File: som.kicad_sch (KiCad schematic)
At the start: 35 parts, among them M1 jetson-orin-nx/nano-module, U4 NTS0102GT

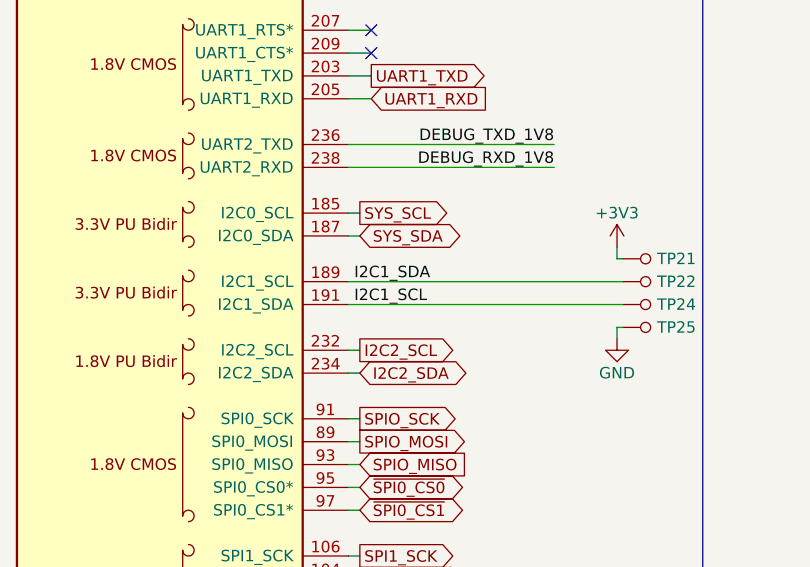
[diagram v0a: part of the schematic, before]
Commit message: Fixed I2C label swap [#40595]
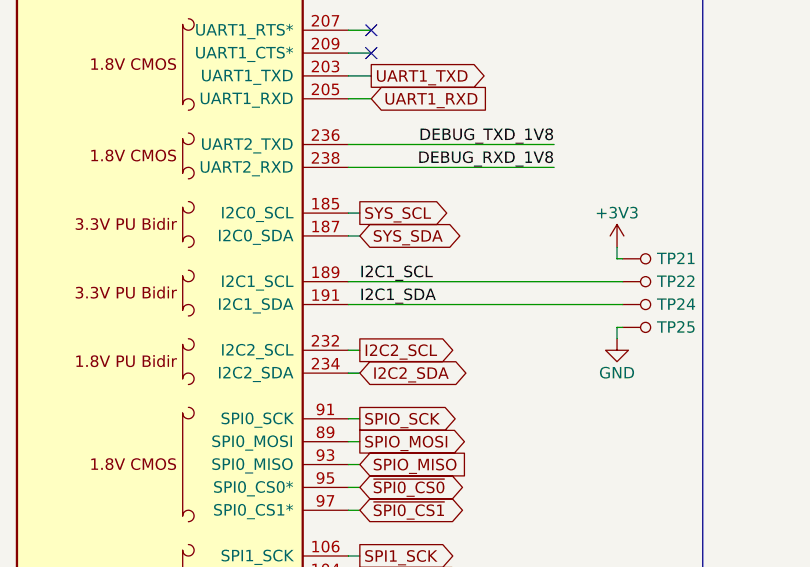
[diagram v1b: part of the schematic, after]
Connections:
- net I2C1_SCL: now also A1.189 (I2C1_SCL), TP22.1; no longer A1.191 (I2C1_SDA), TP24.1
- net I2C1_SDA: now also A1.191 (I2C1_SDA), TP24.1; no longer A1.189 (I2C1_SCL), TP22.1
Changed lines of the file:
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@@
     (effects (font (size 1.27 1.27)) (justify left bottom))
   )
-  (label "I2C1_SCL" (at 189.865 73.66 0)
+  (label "I2C1_SCL" (at 190.5 71.12 0)
     (effects (font (size 1.27 1.27)) (justify left bottom))
   )
-  (label "I2C1_SDA" (at 189.865 71.12 0)
+  (label "I2C1_SDA" (at 190.5 73.66 0)
     (effects (font (size 1.27 1.27)) (justify left bottom))
   )

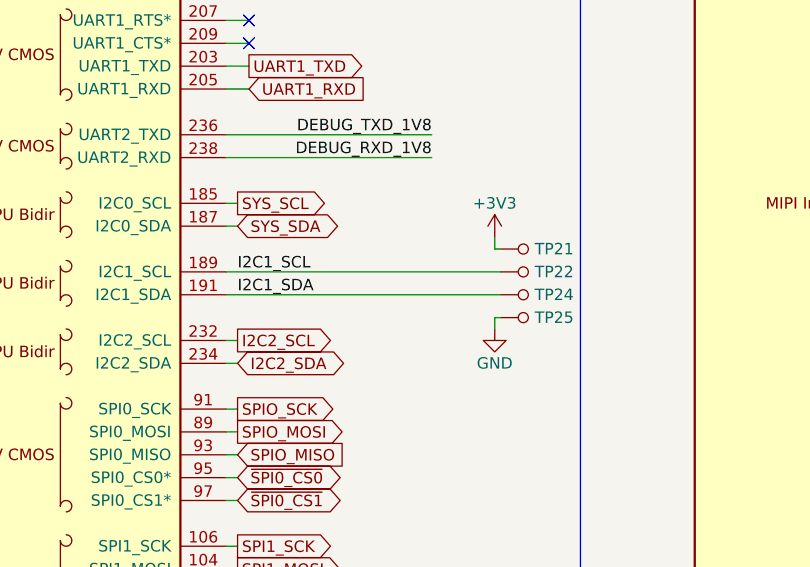
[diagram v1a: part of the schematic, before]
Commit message: Added I2C connector [#40797]
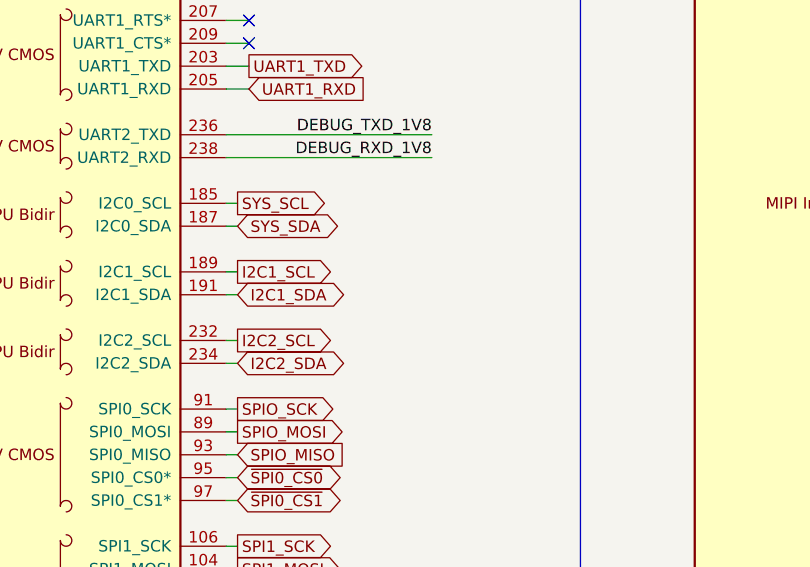
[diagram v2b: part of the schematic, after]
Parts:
- removed TP21, TP22, TP24, TP25: TP_SMD_0_75MM, jetson-orin-baseboard-footprints:Testpoint_smd_0_75mm, symbol jetson-orin-baseboard:TP_SMD_0_75MM
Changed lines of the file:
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@@
     (stroke (width 0) (type default) (color 0 0 0 0))
   )
+  (wire (pts (xy 190.5 73.66) (xy 189.23 73.66))
+    (stroke (width 0) (type default) (color 0 0 0 0))
+  )
   (wire (pts (xy 114.3 35.56) (xy 87.63 35.56))
     (stroke (width 0) (type default) (color 0 0 0 0))
@@
     (stroke (width 0) (type default) (color 0 0 0 0))
   )
-  (wire (pts (xy 219.075 76.2) (xy 219.075 77.47))
-    (stroke (width 0) (type default) (color 0 0 0 0))
-  )
   (wire (pts (xy 189.23 195.58) (xy 194.31 195.58))
     (stroke (width 0) (type default) (color 0 0 0 0))
@@
     (stroke (width 0) (type default) (color 0 0 0 0))
   )
-  (wire (pts (xy 189.23 71.12) (xy 219.71 71.12))
-    (stroke (width 0) (type default) (color 0 0 0 0))
-  )
   (wire (pts (xy 49.53 104.14) (xy 50.8 104.14))
     (stroke (width 0) (type default) (color 0 0 0 0))
@@
     (stroke (width 0) (type default) (color 0 0 0 0))
   )
+  (wire (pts (xy 190.5 71.12) (xy 189.23 71.12))
+    (stroke (width 0) (type default) (color 0 0 0 0))
+  )
   (wire (pts (xy 105.41 64.77) (xy 114.3 64.77))
     (stroke (width 0) (type default) (color 0 0 0 0))
@@
     (stroke (width 0) (type default) (color 0 0 0 0))
   )
-  (wire (pts (xy 219.075 67.31) (xy 219.075 68.58))
-    (stroke (width 0) (type default) (color 0 0 0 0))
-  )
   (wire (pts (xy 49.53 88.9) (xy 50.8 88.9))
     (stroke (width 0) (type default) (color 0 0 0 0))
@@
     (stroke (width 0) (type default) (color 0 0 0 0))
   )
-  (wire (pts (xy 189.23 73.66) (xy 219.71 73.66))
-    (stroke (width 0) (type default) (color 0 0 0 0))
-  )
   (wire (pts (xy 367.03 114.3) (xy 377.19 114.3))
     (stroke (width 0) (type default) (color 0 0 0 0))
@@
     (stroke (width 0) (type default) (color 0 0 0 0))
   )
-  (wire (pts (xy 219.71 76.2) (xy 219.075 76.2))
-    (stroke (width 0) (type default) (color 0 0 0 0))
-  )
   (wire (pts (xy 190.5 104.14) (xy 189.23 104.14))
     (stroke (width 0) (type default) (color 0 0 0 0))
@@
     (stroke (width 0) (type default) (color 0 0 0 0))
   )
-  (wire (pts (xy 219.71 68.58) (xy 219.075 68.58))
-    (stroke (width 0) (type default) (color 0 0 0 0))
-  )
   (wire (pts (xy 377.19 93.98) (xy 367.03 93.98))
     (stroke (width 0) (type default) (color 0 0 0 0))
@@
     (effects (font (size 1.27 1.27)) (justify left bottom))
   )
-  (label "I2C1_SCL" (at 190.5 71.12 0)
-    (effects (font (size 1.27 1.27)) (justify left bottom))
-  )
-  (label "I2C1_SDA" (at 190.5 73.66 0)
-    (effects (font (size 1.27 1.27)) (justify left bottom))
-  )
   (label "SoM_5V_IN" (at 49.53 86.36 180)
     (effects (font (size 1.27 1.27)) (justify right bottom))
@@
     )
   )
+  (global_label "I2C1_SCL" (shape output) (at 190.5 71.12 0)
+    (effects (font (size 1.27 1.27)) (justify left))
+    (property "Intersheet References" "${INTERSHEET_REFS}" (id 0) (at 204.47 71.12 0)
+      (effects (font (size 1.27 1.27)) (justify left))
+    )
+  )
   (global_label "USBSS1_RX_N" (shape output) (at 194.31 205.74 0)
     (effects (font (size 1.27 1.27)) (justify left))
@@
     )
   )
+  (global_label "I2C1_SDA" (shape bidirectional) (at 190.5 73.66 0)
+    (effects (font (size 1.27 1.27)) (justify left))
+    (property "Intersheet References" "${INTERSHEET_REFS}" (id 0) (at 204.47 73.66 0)
+      (effects (font (size 1.27 1.27)) (justify left))
+    )
+  )
   (global_label "USB0_D_N" (shape output) (at 194.31 226.06 0)
     (effects (font (size 1.27 1.27)) (justify left))
@@
     (pin "1")
   )
-  (symbol (lib_id "jetson-orin-baseboard:TP_SMD_0_75MM") (at 222.25 73.66 90) (unit 1)
-    (in_bom yes) (on_board yes) (fields_autoplaced)
-    (property "Reference" "TP24" (id 0) (at 223.52 73.6599 90)
-      (effects (font (size 1.27 1.27)) (justify right))
-    )
-    (property "Value" "TP_SMD_0_75MM" (id 1) (at 224.79 73.66 0)
-      (effects (font (size 1.27 1.27)) hide)
-    )
-    (property "Footprint" "jetson-orin-baseboard-footprints:Testpoint_smd_0_75mm" (id 2) (at 217.17 68.58 0)
-      (effects (font (size 1.524 1.524)) (justify left) hide)
-    )
-    (property "Datasheet" "" (id 3) (at 214.63 68.58 0)
-      (effects (font (size 1.524 1.524)) (justify left) hide)
-    )
-    (pin "1")
-  )
   (symbol (lib_id "jetson-orin-baseboard:GND") (at 30.48 101.6 0) (unit 1)
     (in_bom yes) (on_board yes) (fields_autoplaced)
@@
     (pin "1")
   )
-  (symbol (lib_id "jetson-orin-baseboard:TP_SMD_0_75MM") (at 222.25 76.2 90) (unit 1)
-    (in_bom yes) (on_board yes) (fields_autoplaced)
-    (property "Reference" "TP25" (id 0) (at 223.52 76.1999 90)
-      (effects (font (size 1.27 1.27)) (justify right))
-    )
-    (property "Value" "TP_SMD_0_75MM" (id 1) (at 224.79 76.2 0)
-      (effects (font (size 1.27 1.27)) hide)
-    )
-    (property "Footprint" "jetson-orin-baseboard-footprints:Testpoint_smd_0_75mm" (id 2) (at 217.17 71.12 0)
-      (effects (font (size 1.524 1.524)) (justify left) hide)
-    )
-    (property "Datasheet" "" (id 3) (at 214.63 71.12 0)
-      (effects (font (size 1.524 1.524)) (justify left) hide)
-    )
-    (pin "1")
-  )
   (symbol (lib_id "jetson-orin-baseboard:R_0R_0402") (at 101.6 64.77 0) (unit 1)
     (in_bom yes) (on_board yes)
@@
     (pin "2")
   )
-  (symbol (lib_id "jetson-orin-baseboard:+3V3") (at 219.075 67.31 0) (unit 1)
-    (in_bom yes) (on_board yes)
-    (property "Reference" "#PWR0184" (id 0) (at 219.075 71.12 0)
-      (effects (font (size 1.27 1.27)) hide)
-    )
-    (property "Value" "+3V3" (id 1) (at 219.075 63.5 0))
-    (property "Footprint" "" (id 2) (at 219.075 67.31 0)
-      (effects (font (size 1.27 1.27)) hide)
-    )
-    (property "Datasheet" "" (id 3) (at 219.075 67.31 0)
-      (effects (font (size 1.27 1.27)) hide)
-    )
-    (pin "1")
-  )
   (symbol (lib_id "jetson-orin-baseboard:Jetson-Orin-9.2H-socket") (at 273.05 25.4 0) (mirror y) (unit 2)
     (in_bom yes) (on_board yes)
@@
     (pin "2")
   )
-  (symbol (lib_id "jetson-orin-baseboard:TP_SMD_0_75MM") (at 222.25 71.12 90) (unit 1)
-    (in_bom yes) (on_board yes) (fields_autoplaced)
-    (property "Reference" "TP22" (id 0) (at 223.52 71.1199 90)
-      (effects (font (size 1.27 1.27)) (justify right))
-    )
-    (property "Value" "TP_SMD_0_75MM" (id 1) (at 224.79 71.12 0)
-      (effects (font (size 1.27 1.27)) hide)
-    )
-    (property "Footprint" "jetson-orin-baseboard-footprints:Testpoint_smd_0_75mm" (id 2) (at 217.17 66.04 0)
-      (effects (font (size 1.524 1.524)) (justify left) hide)
-    )
-    (property "Datasheet" "" (id 3) (at 214.63 66.04 0)
-      (effects (font (size 1.524 1.524)) (justify left) hide)
-    )
-    (pin "1")
-  )
   (symbol (lib_id "jetson-orin-baseboard:MS621FE-FL11E") (at 45.72 142.24 0) (mirror y) (unit 1)
     (in_bom yes) (on_board yes) (fields_autoplaced)
@@
     (pin "-")
   )
-  (symbol (lib_id "jetson-orin-baseboard:GND") (at 219.075 77.47 0) (unit 1)
-    (in_bom yes) (on_board yes) (fields_autoplaced)
-    (property "Reference" "#PWR0185" (id 0) (at 219.075 83.82 0)
-      (effects (font (size 1.27 1.27)) hide)
-    )
-    (property "Value" "GND" (id 1) (at 219.075 81.28 0))
-    (property "Footprint" "" (id 2) (at 219.075 77.47 0)
-      (effects (font (size 1.27 1.27)) hide)
-    )
-    (property "Datasheet" "" (id 3) (at 219.075 77.47 0)
-      (effects (font (size 1.27 1.27)) hide)
-    )
-    (pin "1")
-  )
-  (symbol (lib_id "jetson-orin-baseboard:TP_SMD_0_75MM") (at 222.25 68.58 90) (unit 1)
-    (in_bom yes) (on_board yes) (fields_autoplaced)
-    (property "Reference" "TP21" (id 0) (at 223.52 68.5799 90)
-      (effects (font (size 1.27 1.27)) (justify right))
-    )
-    (property "Value" "TP_SMD_0_75MM" (id 1) (at 224.79 68.58 0)
-      (effects (font (size 1.27 1.27)) hide)
-    )
-    (property "Footprint" "jetson-orin-baseboard-footprints:Testpoint_smd_0_75mm" (id 2) (at 217.17 63.5 0)
-      (effects (font (size 1.524 1.524)) (justify left) hide)
-    )
-    (property "Datasheet" "" (id 3) (at 214.63 63.5 0)
-      (effects (font (size 1.524 1.524)) (justify left) hide)
-    )
-    (pin "1")
-  )
   (symbol (lib_id "jetson-orin-baseboard:GND") (at 35.56 101.6 0) (unit 1)

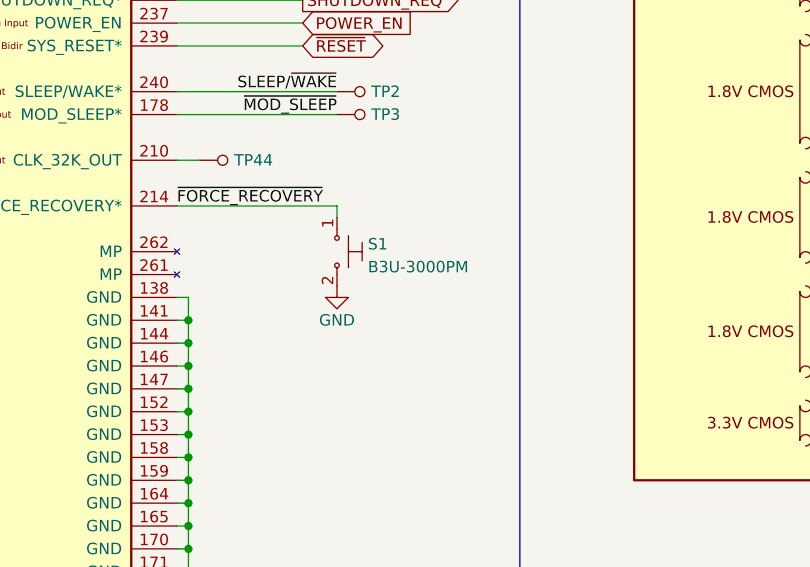
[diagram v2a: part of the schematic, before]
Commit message: Replace buttons with top-actuated ones
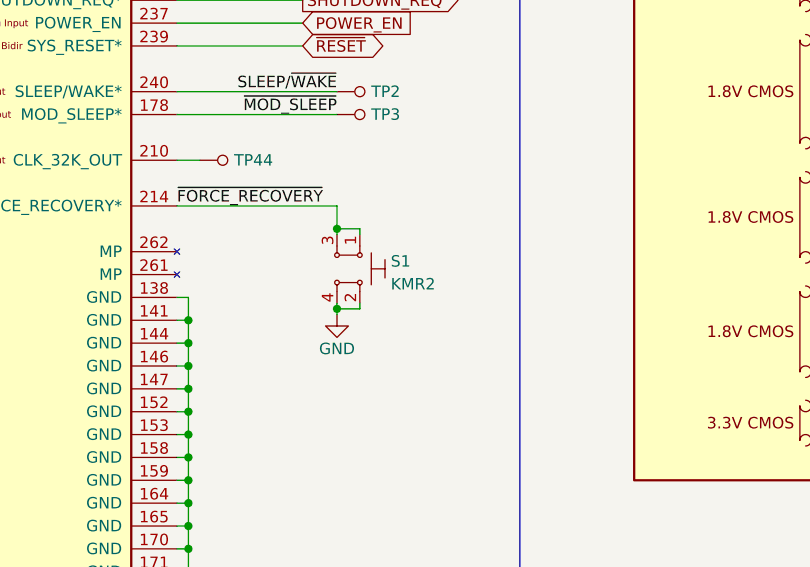
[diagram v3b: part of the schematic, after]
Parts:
- removed S1: B3U-3000PM, jetson-orin-baseboard-footprints:B3U-3000P, symbol jetson-orin-baseboard:B3U-3000PM
- added S1: KMR2, antmicro-footprints:SW_SPST_4.2x2.8, symbol antmicroPushbuttonSwitches:KMR2
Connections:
- net GND: now also S1.2, S1.4
- net ~{FORCE_RECOVERY}: now also S1.1, S1.3
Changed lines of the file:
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@@
   (junction (at 49.53 93.98) (diameter 0) (color 0 0 0 0)
   )
+  (junction (at 119.38 121.92) (diameter 0) (color 0 0 0 0)
+  )
   (junction (at 49.53 180.34) (diameter 0) (color 0 0 0 0)
   )
@@
   (junction (at 49.53 134.62) (diameter 0) (color 0 0 0 0)
   )
+  (junction (at 119.38 130.81) (diameter 0) (color 0 0 0 0)
+  )
   (junction (at 49.53 190.5) (diameter 0) (color 0 0 0 0)
   )
@@
     (stroke (width 0) (type default) (color 0 0 0 0))
   )
+  (wire (pts (xy 119.38 130.175) (xy 119.38 130.81))
+    (stroke (width 0) (type default) (color 0 0 0 0))
+  )
   (wire (pts (xy 377.19 223.52) (xy 367.03 223.52))
     (stroke (width 0) (type default) (color 0 0 0 0))
@@
     (stroke (width 0) (type default) (color 0 0 0 0))
   )
+  (wire (pts (xy 119.38 130.81) (xy 119.38 131.445))
+    (stroke (width 0) (type default) (color 0 0 0 0))
+  )
   (wire (pts (xy 190.5 71.12) (xy 189.23 71.12))
     (stroke (width 0) (type default) (color 0 0 0 0))
@@
     (stroke (width 0) (type default) (color 0 0 0 0))
   )
+  (wire (pts (xy 119.38 121.92) (xy 119.38 122.555))
+    (stroke (width 0) (type default) (color 0 0 0 0))
+  )
   (wire (pts (xy 101.6 129.54) (xy 102.87 129.54))
     (stroke (width 0) (type default) (color 0 0 0 0))
@@
     (stroke (width 0) (type default) (color 0 0 0 0))
   )
+  (wire (pts (xy 119.38 121.92) (xy 121.92 121.92))
+    (stroke (width 0) (type default) (color 0 0 0 0))
+  )
   (wire (pts (xy 114.3 38.1) (xy 87.63 38.1))
     (stroke (width 0) (type default) (color 0 0 0 0))
@@
     (stroke (width 0) (type default) (color 0 0 0 0))
   )
+  (wire (pts (xy 121.92 121.92) (xy 121.92 122.555))
+    (stroke (width 0) (type default) (color 0 0 0 0))
+  )
   (wire (pts (xy 93.98 250.19) (xy 93.98 251.46))
     (stroke (width 0) (type default) (color 0 0 0 0))
@@
     (stroke (width 0) (type default) (color 0 0 0 0))
   )
+  (wire (pts (xy 119.38 130.81) (xy 121.92 130.81))
+    (stroke (width 0) (type default) (color 0 0 0 0))
+  )
   (wire (pts (xy 377.19 149.86) (xy 367.03 149.86))
     (stroke (width 0) (type default) (color 0 0 0 0))
@@
     (stroke (width 0) (type default) (color 0 0 0 0))
   )
+  (wire (pts (xy 121.92 130.81) (xy 121.92 130.175))
+    (stroke (width 0) (type default) (color 0 0 0 0))
+  )
   (wire (pts (xy 49.53 182.88) (xy 49.53 180.34))
     (stroke (width 0) (type default) (color 0 0 0 0))
@@
     (stroke (width 0) (type default) (color 0 0 0 0))
   )
+  (wire (pts (xy 119.38 119.38) (xy 119.38 121.92))
+    (stroke (width 0) (type default) (color 0 0 0 0))
+  )
   (wire (pts (xy 101.6 193.04) (xy 102.87 193.04))
     (stroke (width 0) (type default) (color 0 0 0 0))
@@
     (stroke (width 0) (type default) (color 0 0 0 0))
   )
-  (wire (pts (xy 119.38 119.38) (xy 119.38 120.65))
-    (stroke (width 0) (type default) (color 0 0 0 0))
-  )
   (wire (pts (xy 189.23 243.84) (xy 194.31 243.84))
     (stroke (width 0) (type default) (color 0 0 0 0))
@@
     (pin "1")
   )
+  (symbol (lib_id "antmicroPushbuttonSwitches:KMR2") (at 121.92 126.365 270) (unit 1)
+    (in_bom yes) (on_board yes) (fields_autoplaced)
+    (property "Reference" "S1" (id 0) (at 125.349 125.5303 90)
+      (effects (font (size 1.27 1.27)) (justify left))
+    )
+    (property "Value" "KMR2" (id 1) (at 125.349 128.0672 90)
+      (effects (font (size 1.27 1.27)) (justify left))
+    )
+    (property "Footprint" "antmicro-footprints:SW_SPST_4.2x2.8" (id 2) (at 127 131.445 0)
+      (effects (font (size 1.27 1.27)) (justify left) hide)
+    )
+    (property "Datasheet" "http://www.farnell.com/datasheets/2631211.pdf" (id 3) (at 129.54 131.445 0)
+      (effects (font (size 1.524 1.524)) (justify left) hide)
+    )
+    (property "MPN" "KMR211NGLFS" (id 4) (at 131.9022 131.3434 0)
+      (effects (font (size 1.524 1.524)) (justify left) hide)
+    )
+    (property "Manufacturer" "C&K Components" (id 5) (at 133.9088 131.445 0)
+      (effects (font (size 1.524 1.524)) (justify left) hide)
+    )
+    (pin "1")
+    (pin "2")
+    (pin "3")
+    (pin "4")
+  )
   (symbol (lib_id "jetson-orin-baseboard:jetson-orin-nx{slash}nano-module") (at 189.23 275.59 0) (unit 1)
     (in_bom yes) (on_board yes) (fields_autoplaced)
@@
     (pin "1")
   )
-  (symbol (lib_id "jetson-orin-baseboard:B3U-3000PM") (at 119.38 124.46 270) (unit 1)
-    (in_bom yes) (on_board yes) (fields_autoplaced)
-    (property "Reference" "S1" (id 0) (at 122.809 123.6253 90)
-      (effects (font (size 1.27 1.27)) (justify left))
-    )
-    (property "Value" "B3U-3000PM" (id 1) (at 122.809 126.1622 90)
-      (effects (font (size 1.27 1.27)) (justify left))
-    )
-    (property "Footprint" "jetson-orin-baseboard-footprints:B3U-3000P" (id 2) (at 124.46 129.54 0)
-      (effects (font (size 1.27 1.27)) (justify left) hide)
-    )
-    (property "Datasheet" "http://www.farnell.com/datasheets/2610940.pdf" (id 3) (at 127 129.54 0)
-      (effects (font (size 1.524 1.524)) (justify left) hide)
-    )
-    (property "MPN" "B3U-3000PM" (id 4) (at 129.3622 129.4384 0)
-      (effects (font (size 1.524 1.524)) (justify left) hide)
-    )
-    (property "Manufacturer" "OMRON" (id 5) (at 131.3688 129.54 0)
-      (effects (font (size 1.524 1.524)) (justify left) hide)
-    )
-    (pin "1")
-    (pin "2")
-  )
   (symbol (lib_id "jetson-orin-baseboard:R_0R_0402") (at 287.02 109.22 0) (mirror x) (unit 1)
     (in_bom yes) (on_board yes)
@@
     (pin "1")
   )
-  (symbol (lib_id "jetson-orin-baseboard:GND") (at 119.38 128.27 0) (unit 1)
+  (symbol (lib_id "jetson-orin-baseboard:GND") (at 119.38 131.445 0) (unit 1)
     (in_bom yes) (on_board yes) (fields_autoplaced)
-    (property "Reference" "#PWR017" (id 0) (at 119.38 134.62 0)
+    (property "Reference" "#PWR017" (id 0) (at 119.38 137.795 0)
       (effects (font (size 1.27 1.27)) hide)
     )
-    (property "Value" "GND" (id 1) (at 119.38 132.08 0))
-    (property "Footprint" "" (id 2) (at 119.38 128.27 0)
+    (property "Value" "GND" (id 1) (at 119.38 135.255 0))
+    (property "Footprint" "" (id 2) (at 119.38 131.445 0)
       (effects (font (size 1.27 1.27)) hide)
     )
-    (property "Datasheet" "" (id 3) (at 119.38 128.27 0)
+    (property "Datasheet" "" (id 3) (at 119.38 131.445 0)
       (effects (font (size 1.27 1.27)) hide)
     )
